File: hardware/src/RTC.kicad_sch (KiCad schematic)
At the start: 0 parts

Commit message: Add: RTC schematic
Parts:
- added BT401: Battery_Cell, symbol Device:Battery_Cell
- added C401, C403: 10µF, symbol Device:C
- added C402, C404: 0.1µF, symbol Device:C
- added U401: DS3231M, Package_SO:SOIC-16W_7.5x10.3mm_P1.27mm, symbol Timer_RTC:DS3231M
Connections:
- new net +3V3: C401.1, C402.1, U401.2 (VCC)
- new net +BATT: BT401.1 (+), C403.1, C404.1, U401.14 (VBAT)
- new net 32kHz: U401.1 (32KHZ)
- new net GND: BT401.2 (-), C401.2, C402.2, C403.2, C404.2, U401.10 (GND), U401.11 (GND), U401.12 (GND), U401.13 (GND), U401.5 (GND), U401.6 (GND), U401.7 (GND), U401.8 (GND), U401.9 (GND)
- new net I^{2}C.SCL: U401.16 (SCL)
- new net I^{2}C.SDA: U401.15 (SDA)
- new net ~{INT}_{RTC}: U401.3 (~{INT}/SQW)
- new net ~{RST}_{RTC}: U401.4 (~{RST})
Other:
- title: Wordclock - RTC -> Wordclock - Real Time Clock

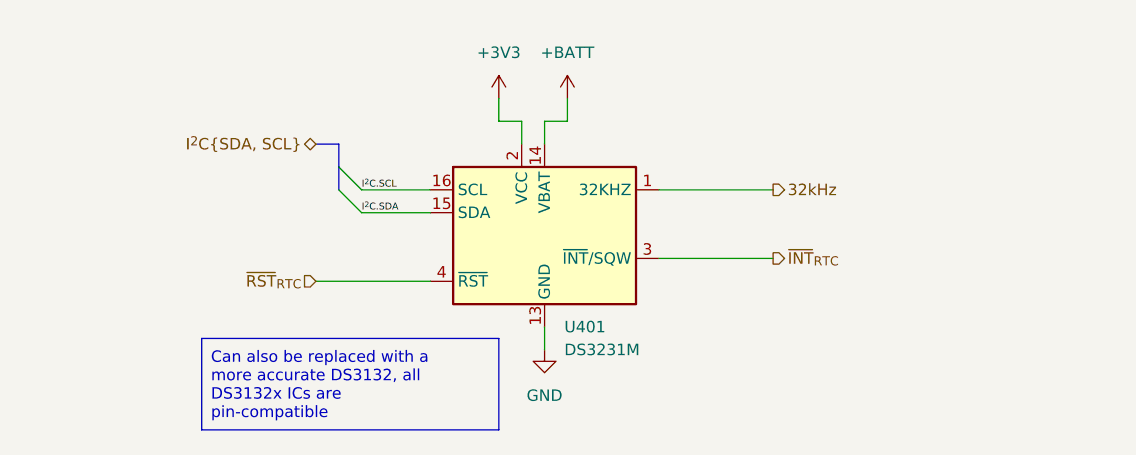
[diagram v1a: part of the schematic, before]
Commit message: Mod: RTC GPIOs
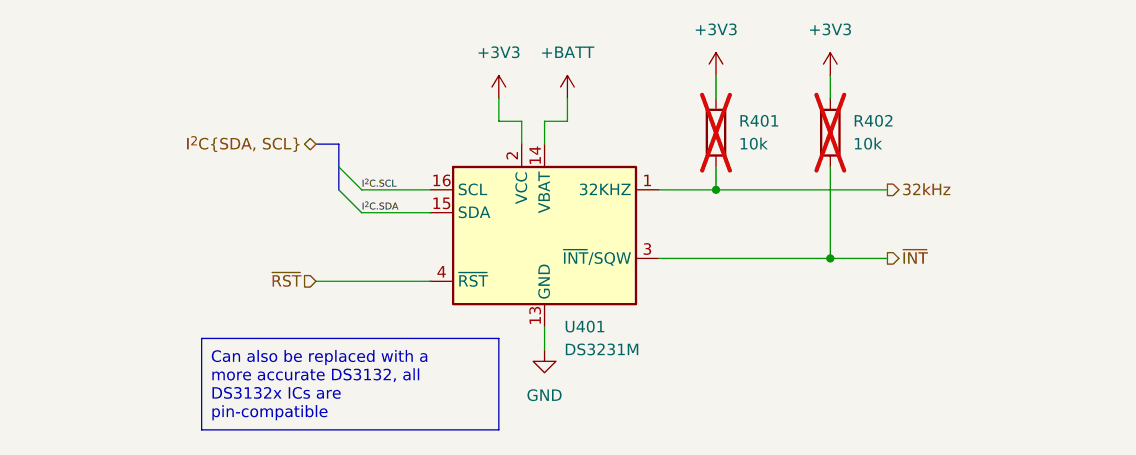
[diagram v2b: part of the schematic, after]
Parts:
- added R401, R402: 10k, symbol Device:R
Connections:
- net +3V3: now also R401.1, R402.1
- net 32kHz: now also R401.2
- net ~{INT}_{RTC} renamed ~{INT}
- net ~{INT}: now also R402.2
- net ~{RST}_{RTC} renamed ~{RST}

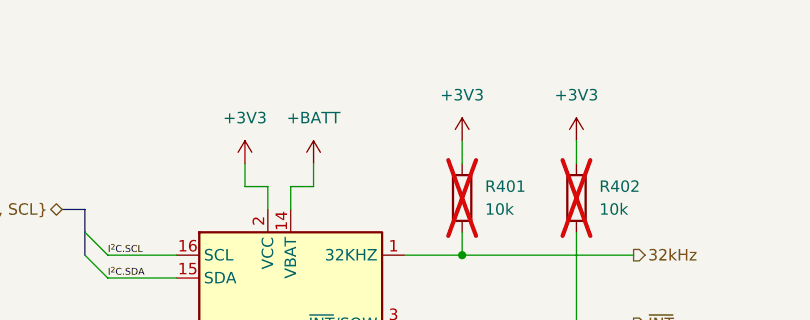
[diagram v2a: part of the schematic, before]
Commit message: Add: Text Headers to the indidual schematic regions
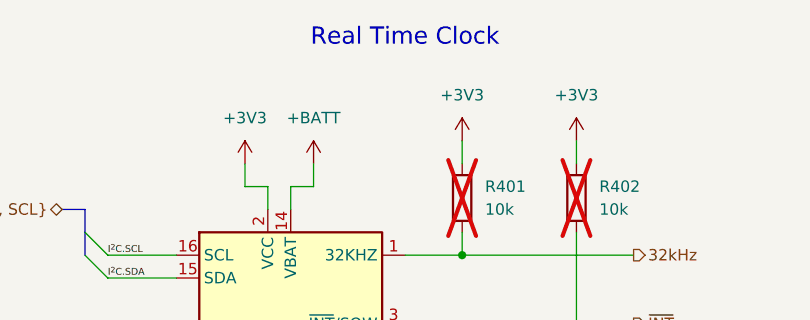
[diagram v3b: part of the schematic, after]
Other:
- note added: "Real Time Clock"
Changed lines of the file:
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@@
+		)
+	)
+	(text "Real Time Clock"
+		(exclude_from_sim no)
+		(at 127 57.15 0)
+		(effects
+			(font
+				(size 1.905 1.905)
+			)
 		)
 	)

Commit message: Mod: Changed date and made some small corrections
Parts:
- C403: value 10µF -> 1µF; now not fitted
- C404: now not fitted
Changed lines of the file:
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@@
 	(title_block
 		(title "Wordclock - Real Time Clock")
-		(date "2024-10-20")
+		(date "2024-10-21")
 		(rev "A")
 		(company "ElektroNik Zoller")
@@
 		(in_bom yes)
 		(on_board yes)
-		(dnp no)
+		(dnp yes)
 		(fields_autoplaced yes)
 		(property "Reference" "C404"
@@
 		)
 		(property "Description" "Unpolarized capacitor"
+			(at 165.1 177.8 0)
+			(effects
+				(font
+					(size 1.27 1.27)
+				)
+				(hide yes)
+			)
+		)
+		(property "Manufacturer" ""
+			(at 165.1 177.8 0)
+			(effects
+				(font
+					(size 1.27 1.27)
+				)
+				(hide yes)
+			)
+		)
+		(property "Manufacturer Part no." ""
+			(at 165.1 177.8 0)
+			(effects
+				(font
+					(size 1.27 1.27)
+				)
+				(hide yes)
+			)
+		)
+		(property "Vendor 1" ""
+			(at 165.1 177.8 0)
+			(effects
+				(font
+					(size 1.27 1.27)
+				)
+				(hide yes)
+			)
+		)
+		(property "Vendor 1 Part no." ""
+			(at 165.1 177.8 0)
+			(effects
+				(font
+					(size 1.27 1.27)
+				)
+				(hide yes)
+			)
+		)
+		(property "Vendor 2" ""
+			(at 165.1 177.8 0)
+			(effects
+				(font
+					(size 1.27 1.27)
+				)
+				(hide yes)
+			)
+		)
+		(property "Vendor 2 Part no." ""
+			(at 165.1 177.8 0)
+			(effects
+				(font
+					(size 1.27 1.27)
+				)
+				(hide yes)
+			)
+		)
+		(property "Internal 1 Part no." ""
+			(at 165.1 177.8 0)
+			(effects
+				(font
+					(size 1.27 1.27)
+				)
+				(hide yes)
+			)
+		)
+		(property "Internal 2 Part no." ""
 			(at 165.1 177.8 0)
 			(effects
@@
 		(in_bom yes)
 		(on_board yes)
-		(dnp no)
+		(dnp yes)
 		(fields_autoplaced yes)
 		(property "Reference" "C403"
@@
 			)
 		)
-		(property "Value" "10µF"
+		(property "Value" "1µF"
 			(at 156.21 179.0699 0)
 			(effects
@@
 			(at 152.4 177.8 0)
 			(effects
+				(font
+					(size 1.27 1.27)
+				)
+				(hide yes)
+			)
+		)
+		(property "Manufacturer" ""
+			(at 152.4 177.8 0)
+			(effects
+				(font
+					(size 1.27 1.27)
+				)
+				(hide yes)
+			)
+		)
+		(property "Manufacturer Part no." ""
+			(at 152.4 177.8 0)
+			(effects
+				(font
+					(size 1.27 1.27)
+				)
+				(hide yes)
+			)
+		)
+		(property "Vendor 1" ""
+			(at 152.4 177.8 0)
+			(effects
+				(font
+					(size 1.27 1.27)
+				)
+				(hide yes)
+			)
+		)
+		(property "Vendor 1 Part no." ""
+			(at 152.4 177.8 0)
+			(effects
+				(font
+					(size 1.27 1.27)
+				)
+				(hide yes)
+			)
+		)
+		(property "Vendor 2" ""
+			(at 152.4 177.8 0)
+			(effects
+				(font
+					(size 1.27 1.27)
+				)
+				(hide yes)
+			)
+		)
+		(property "Vendor 2 Part no." ""
+			(at 152.4 177.8 0)
+			(effects
+				(font
+					(size 1.27 1.27)
+				)
+				(hide yes)
+			)
+		)
+		(property "Internal 1 Part no." ""
+			(at 152.4 177.8 0)
+			(effects
+				(font
+					(size 1.27 1.27)
+				)
+				(hide yes)
+			)
+		)
+		(property "Internal 2 Part no." ""
+			(at 152.4 177.8 0)
+			(effects

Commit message: Add: Brightness sensors to the schematic
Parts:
- added R403: 0R, symbol Device:R
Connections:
- net ~{RST}: now also R403.2; no longer U401.4 (~{RST})
- new net: R403.1, U401.4 (~{RST})
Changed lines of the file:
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@@
 	(wire
 		(pts
-			(xy 88.9 91.44) (xy 101.6 91.44)
+			(xy 76.2 91.44) (xy 85.09 91.44)
 		)
 		(stroke
@@
 		)
 	)
+	(wire
+		(pts
+			(xy 92.71 91.44) (xy 101.6 91.44)
+		)
+		(stroke
+			(width 0)
+			(type default)
+		)
+	)
 	(text_box "Can also be replaced with a more accurate DS3132, all DS3132x ICs are pin-compatible"
 		(exclude_from_sim no)
-		(at 76.2 97.79 0)
+		(at 127 95.25 0)
 		(size 33.02 10.16)
 		(stroke
@@
 			)
 			(justify left)
+		)
+	)
+	(text_box "The RST circuit via the CP2102 circuit still needs to be tested!"
+		(exclude_from_sim no)
+		(at 76.2 95.25 0)
+		(size 19.05 11.43)
+		(stroke
+			(width 0)
+			(type default)
+		)
+		(fill
+			(type none)
+		)
+		(effects
+			(font
+				(size 1.27 1.27)
+			)
+			(justify left top)
 		)
 	)
@@
 	(hierarchical_label "~{RST}"
 		(shape input)
-		(at 88.9 91.44 180)
+		(at 76.2 91.44 180)
 		(fields_autoplaced yes)
 		(effects
@@
 					(unit 1)
 				)
+			)
+		)
+	)
+	(symbol
+		(lib_id "Device:R")
+		(at 88.9 91.44 270)
+		(unit 1)
+		(exclude_from_sim no)
+		(in_bom yes)
+		(on_board yes)
+		(dnp yes)
+		(property "Reference" "R403"
+			(at 85.598 90.17 90)
+			(effects
+				(font
+					(size 1.27 1.27)
+				)
+				(justify right)
+			)
+		)
+		(property "Value" "0R"
+			(at 92.456 90.17 90)
+			(effects
+				(font
+					(size 1.27 1.27)
+				)
+				(justify left)
+			)
+		)
+		(property "Footprint" ""
+			(at 88.9 89.662 90)
+			(effects
+				(font
+					(size 1.27 1.27)
+				)
+				(hide yes)
+			)
+		)
+		(property "Datasheet" "~"
+			(at 88.9 91.44 0)
+			(effects
+				(font
+					(size 1.27 1.27)
+				)
+				(hide yes)
+			)
+		)
+		(property "Description" "Resistor"
+			(at 88.9 91.44 0)
+			(effects
+				(font
+					(size 1.27 1.27)
+				)
+				(hide yes)
+			)
+		)
+		(property "Manufacturer" ""
+			(at 88.9 91.44 0)
+			(effects
+				(font
+					(size 1.27 1.27)
+				)
+				(hide yes)
+			)
+		)
+		(property "Manufacturer Part no." ""
+			(at 88.9 91.44 0)
+			(effects
+				(font
+					(size 1.27 1.27)
+				)
+				(hide yes)
+			)
+		)
+		(property "Vendor 1" ""
+			(at 88.9 91.44 0)
+			(effects
+				(font
+					(size 1.27 1.27)
+				)
+				(hide yes)
+			)
+		)
+		(property "Vendor 1 Part no." ""
+			(at 88.9 91.44 0)
+			(effects
+				(font
+					(size 1.27 1.27)
+				)
+				(hide yes)
+			)
+		)
+		(property "Vendor 2" ""
+			(at 88.9 91.44 0)
+			(effects
+				(font
+					(size 1.27 1.27)
+				)
+				(hide yes)
+			)
+		)
+		(property "Vendor 2 Part no." ""
+			(at 88.9 91.44 0)
+			(effects
+				(font
+					(size 1.27 1.27)
+				)
+				(hide yes)
+			)
+		)
+		(property "Internal 1 Part no." ""
+			(at 88.9 91.44 0)
+			(effects
+				(font
+					(size 1.27 1.27)
+				)
+				(hide yes)
+			)
+		)
+		(property "Internal 2 Part no." ""
+			(at 88.9 91.44 0)
+			(effects
+				(font
+					(size 1.27 1.27)
+				)
+				(hide yes)
+			)
+		)
+		(pin "2"
+		)
+		(pin "1"
+		)
+		(instances
+			(project "ESP-Wordclock"
+				(path "/bfaac094-0365-40a4-8b7a-d4d62ace544e/ec66bd8a-ab18-419c-8a8f-29e1d0925890"
+					(reference "R403")
+					(unit 1)
+				)
